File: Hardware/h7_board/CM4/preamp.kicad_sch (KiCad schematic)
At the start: 25 parts, among them IC1 OPA659IDBVR, IC2 OPA659IDBVR, IC3 LMH6643MAX_NOPB, J1 Conn_Coaxial, J5 PREAMP, J6 BIASED OUTPUT

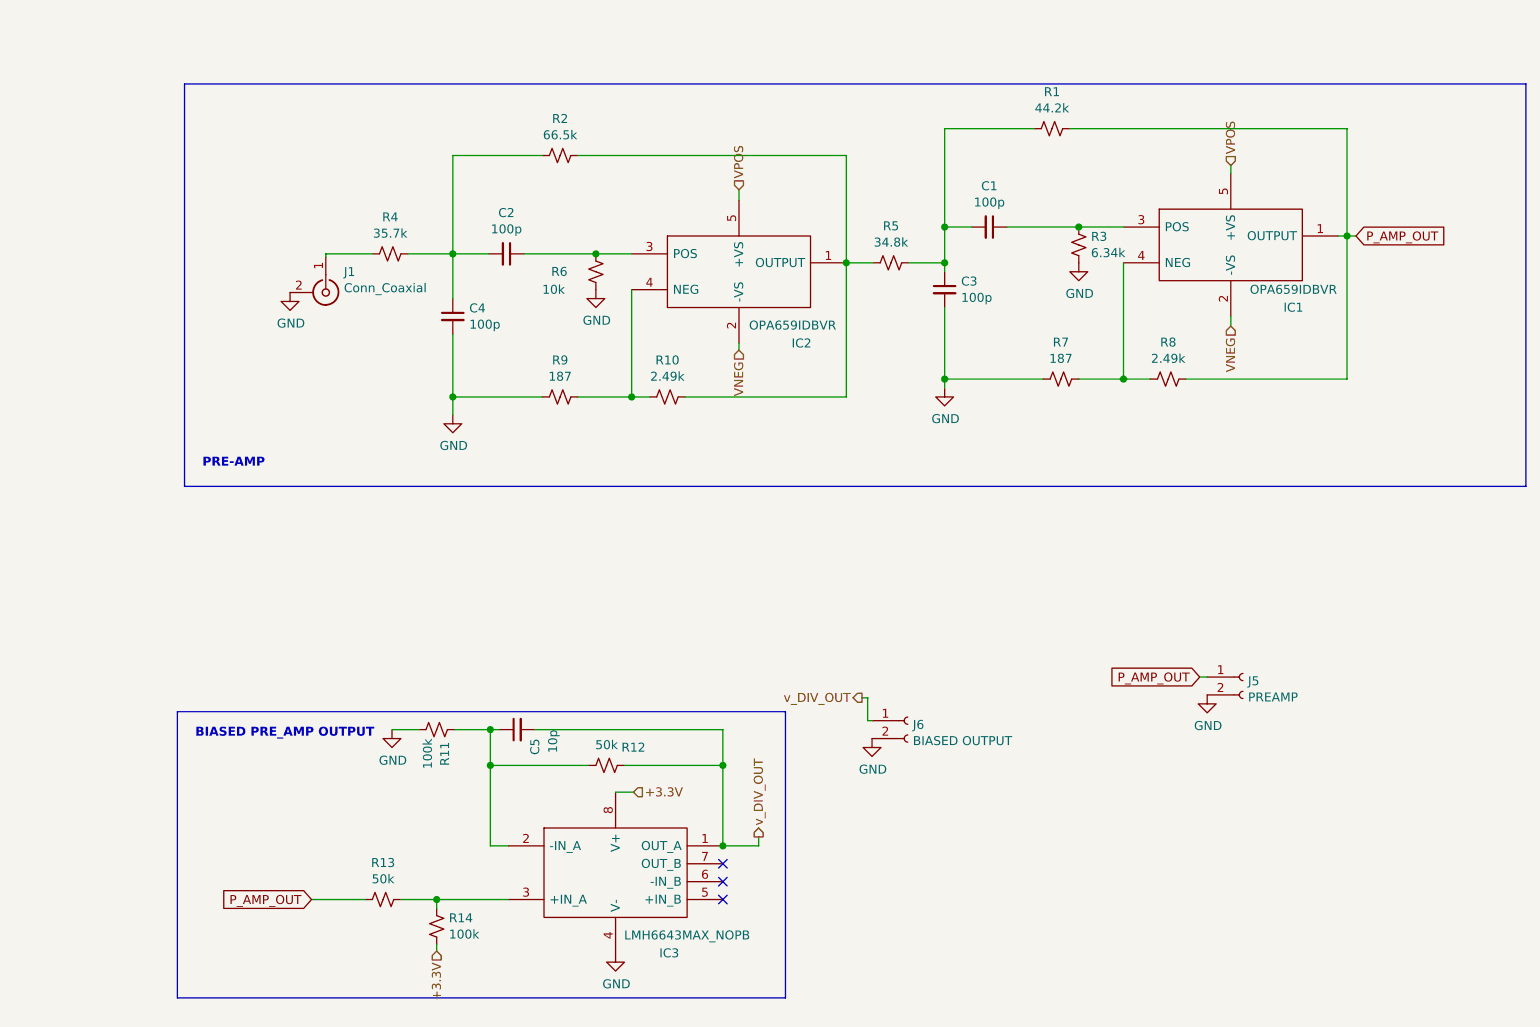
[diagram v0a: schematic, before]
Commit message: Edited Design to modify to LDO regulator and improve board layout
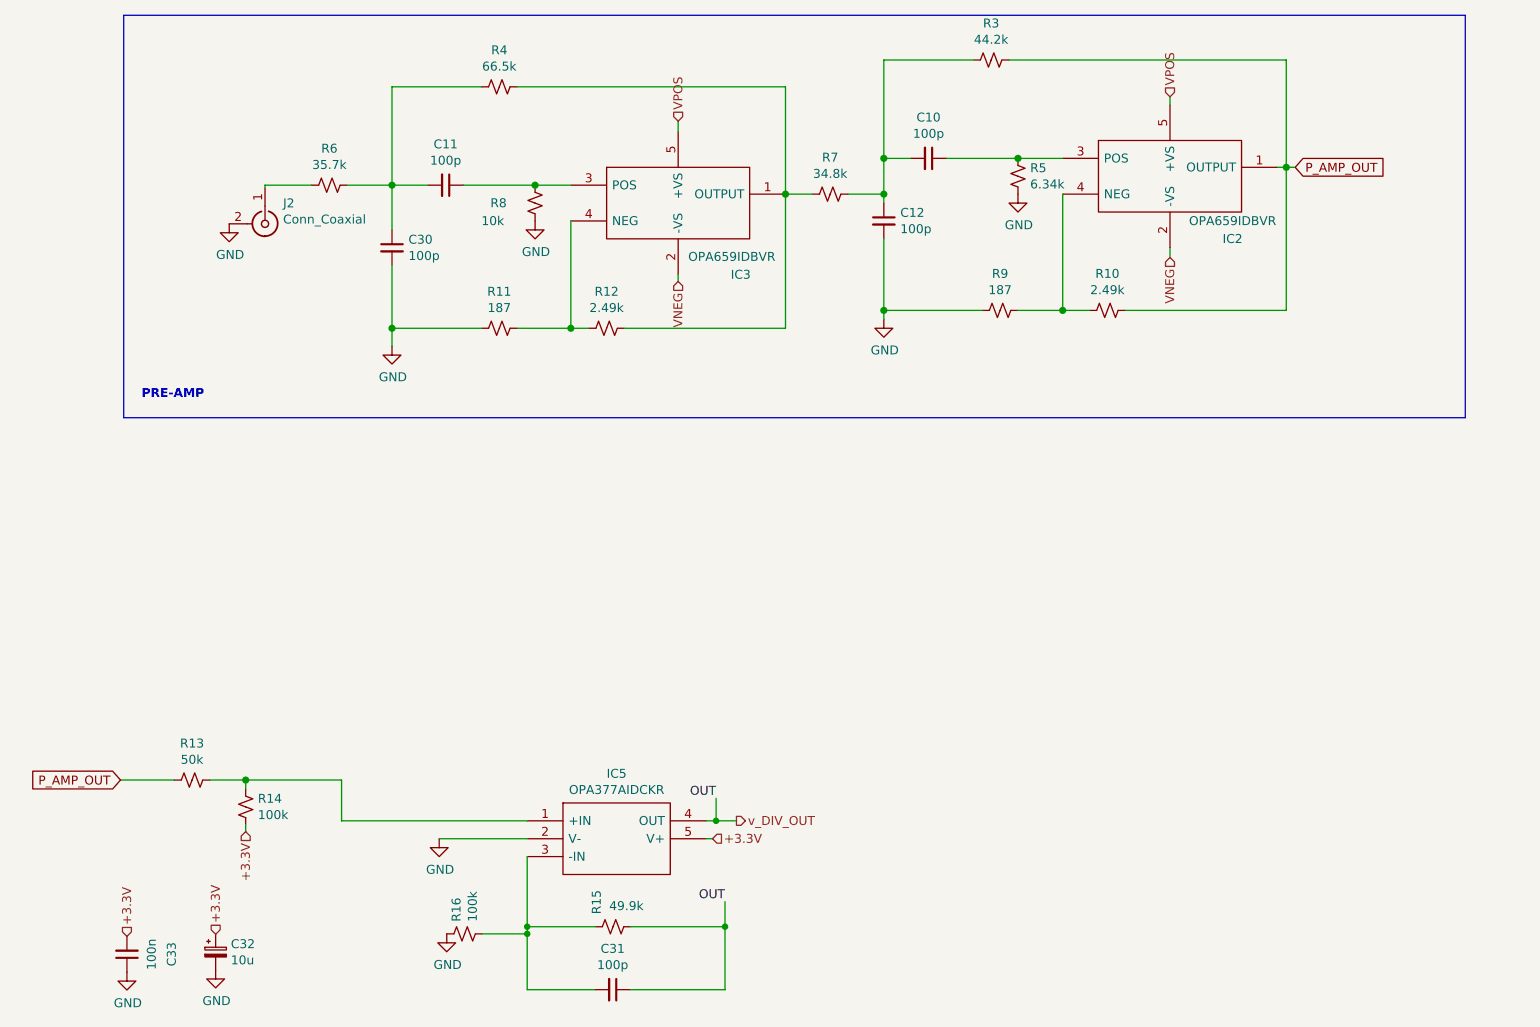
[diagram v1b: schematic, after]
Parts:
- removed C1, C2, C3, C4: 100p, Capacitor_SMD:C_0402_1005Metric, symbol Device:C_Small
- removed C5: 10p, Capacitor_SMD:C_0402_1005Metric, symbol Device:C_Small
- removed IC1: OPA659IDBVR, SamacSys_Parts:SOT95P280X145-5N, symbol SamacSys_Parts:OPA659IDBVR
- removed IC3: LMH6643MAX_NOPB, SamacSys_Parts:SOIC127P600X175-8N, symbol SamacSys_Parts:LMH6643MAX_NOPB
- removed J1: Conn_Coaxial, Connector_Coaxial:SMA_Wurth_60312002114503_Vertical, symbol Connector:Conn_Coaxial
- removed J5: PREAMP, Connector_PinHeader_2.54mm:PinHeader_1x02_P2.54mm_Horizontal, symbol Connector:Conn_01x02_Female
- removed J6: BIASED OUTPUT, Connector_PinHeader_2.54mm:PinHeader_1x02_P2.54mm_Horizontal, symbol Connector:Conn_01x02_Female
- removed R1: 44.2k, Resistor_SMD:R_0402_1005Metric, symbol Device:R_Small_US
- removed R2: 66.5k, Resistor_SMD:R_0402_1005Metric, symbol Device:R_Small_US
- added C10, C11, C12, C30, C31: 100p, Capacitor_SMD:C_0402_1005Metric, symbol Device:C_Small
- added C32: 10u, Capacitor_Tantalum_SMD:CP_EIA-3216-18_Kemet-A, symbol Device:C_Polarized_Small
- added C33: 100n, Capacitor_SMD:C_0402_1005Metric, symbol Device:C_Small
- added IC3: OPA659IDBVR, SamacSys_Parts:SOT95P280X145-5N, symbol SamacSys_Parts:OPA659IDBVR
- added IC5: OPA377AIDCKR, SamacSys_Parts:SOT65P210X110-5N, symbol SamacSys_Parts:OPA377AIDCKR
- added J2: Conn_Coaxial, Connector_Coaxial:SMA_Wurth_60312002114503_Vertical, symbol Connector:Conn_Coaxial
- added R15: 49.9k, Resistor_SMD:R_0603_1608Metric, symbol Device:R_Small_US
- added R16: 100k, Resistor_SMD:R_0603_1608Metric, symbol Device:R_Small_US
- R11: value 100k -> 187; footprint Resistor_SMD:R_0603_1608Metric -> Resistor_SMD:R_0402_1005Metric; LCSC Part # C25803 -> C39887
- R12: value 50k -> 2.49k; footprint Resistor_SMD:R_0603_1608Metric -> Resistor_SMD:R_0402_1005Metric; LCSC Part # C23184 -> C25884
- R3: value 6.34k -> 44.2k; LCSC Part # C45013 -> C25895
- R4: value 35.7k -> 66.5k; LCSC Part # C26975 -> C29381
- R5: value 34.8k -> 6.34k; LCSC Part # C47493 -> C45013
- R6: value 10k -> 35.7k; LCSC Part # C25744 -> C26975
- R7: value 187 -> 34.8k; LCSC Part # C39887 -> C47493
- R8: value 2.49k -> 10k; LCSC Part # C25884 -> C25744
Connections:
- net +3.3V: now also C32.1, C33.2, IC5.5 (V+)
- net GND: now also R11.2, R5.1, R8.1, C12.2, C30.2, C32.2, C33.1, IC5.2 (V-), J2.2 (Ext), R16.2; no longer R11.1, R3.1, R6.1, R7.2
- net P_AMP_OUT: now also IC2.1 (OUTPUT), R10.1, R3.1; no longer R8.1
- net VNEG: now also IC3.2 (-VS)
- net VPOS: now also IC3.5 (+VS)
- net v_DIV_OUT: now also C31.1, IC5.4 (OUT), R15.1; no longer R12.1
- net at R7.1: now also R3.2, C10.2, C12.1; no longer R8.2
- net at R4.1: now also R12.1, R7.2, IC3.1 (OUTPUT)
- net at R4.2: now also R6.1, C11.2, C30.1
- net at R12.2: now also R11.1, IC3.4 (NEG); no longer R11.2
- net at R13.1, R14.2: now also IC5.1 (+IN)
- net at IC2.3 (POS): now also R5.2, C10.1; no longer R6.2
- new net: C31.2, IC5.3 (-IN), R15.2, R16.1
- new net: C11.1, IC3.3 (POS), R8.2
- new net: J2.1 (In), R6.2
- no-connect marks 3 -> 0
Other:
- note removed: "BIASED PRE_AMP OUTPUT"

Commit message: Added Low noise analysis and design files
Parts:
- C32: LCSC Part # (none) -> C7171
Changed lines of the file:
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@@
+      (effects (font (size 1.27 1.27)) hide)
+    )
+    (property "LCSC Part #" "C7171" (id 4) (at 45.3136 160.274 0)
       (effects (font (size 1.27 1.27)) hide)
     )
